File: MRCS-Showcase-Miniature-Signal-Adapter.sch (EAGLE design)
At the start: 4 parts

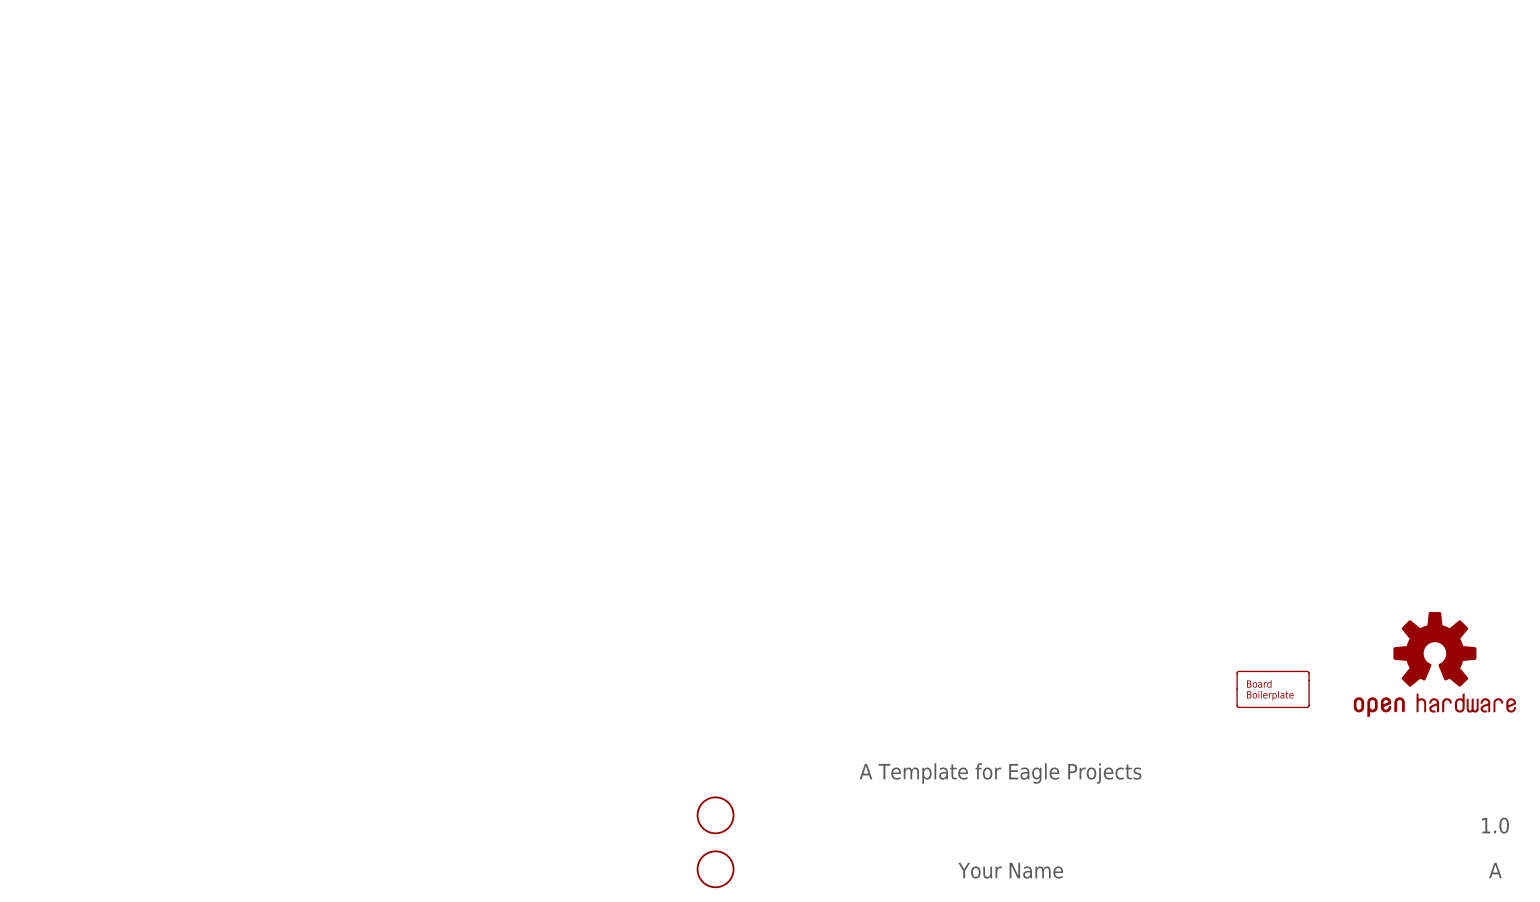
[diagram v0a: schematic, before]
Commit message: Various adjustments of hole and chip sizes
- changed SMD resistors to 1206 to allow easier soldering
- Changed size of shaft hole to match #52 drill
- changes pads to .6mm for better fit with #24 wire
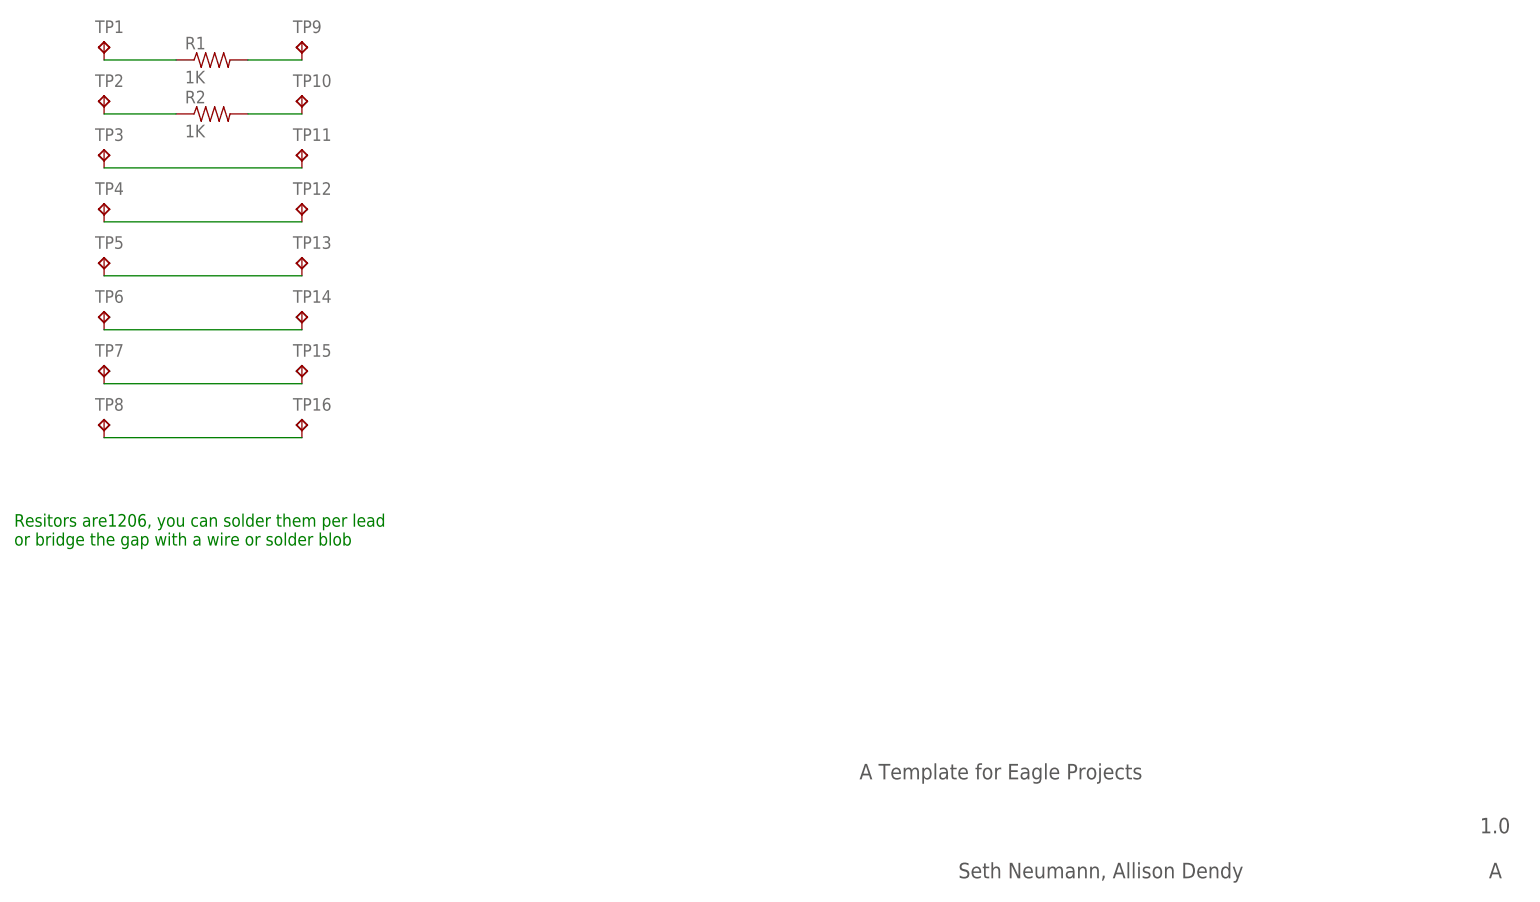
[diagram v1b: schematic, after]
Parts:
- removed BOARD1: BOARD80X100, SPCoast:BOARD80X100
- removed FID1, FID2: FIDUCIAL, SPCoast:FIDUCIAL
- removed OSHW1: DOC-OSHW-LOGO-M, SPCoast:DOC-OSHW-LOGO-M
- added R1, R2: 1K, SPCoast:R1206
- added TP1, TP10, TP11, TP12, TP13, TP14, TP15, TP16, TP2, TP3, TP4, TP5, TP6, TP7, TP8, TP9: TP, MRCS:TP
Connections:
- new net N$10: TP16.TP, TP8.TP
- new net N$17: R1.2, TP9.TP
- new net N$2: R1.1, TP1.TP
- new net N$3: R2.1, TP2.TP
- new net N$4: R2.2, TP10.TP
- new net N$5: TP11.TP, TP3.TP
- new net N$6: TP12.TP, TP4.TP
- new net N$7: TP13.TP, TP5.TP
- new net N$8: TP14.TP, TP6.TP
- new net N$9: TP15.TP, TP7.TP
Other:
- note added: "Resitors are1206, you can solder them per lead or bridge the gap with a wire or solder blob"
- note added: "Seth Neumann, Allison Dendy"
- note removed: "Your Name"
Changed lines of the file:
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@@
 <parts>
 <part name="FRAME1" library="SPCoast" deviceset="DOC-FRAME-LETTER" device=""/>
-<part name="OSHW1" library="SPCoast" deviceset="DOC-OSHW-LOGO-" device="M"/>
-<part name="BOARD1" library="SPCoast" deviceset="BOARD" device="80X100"/>
-<part name="FID2" library="SPCoast" deviceset="FIDUCIAL" device=""/>
-<part name="FID1" library="SPCoast" deviceset="FIDUCIAL" device=""/>
+<part name="R1" library="SPCoast" deviceset="R*" device="1206" value="1K"/>
+<part name="R2" library="SPCoast" deviceset="R*" device="1206" value="1K"/>
+<part name="TP1" library="MRCS" deviceset="TP" device=""/>
+<part name="TP2" library="MRCS" deviceset="TP" device=""/>
+<part name="TP3" library="MRCS" deviceset="TP" device=""/>
+<part name="TP4" library="MRCS" deviceset="TP" device=""/>
+<part name="TP5" library="MRCS" deviceset="TP" device=""/>
+<part name="TP6" library="MRCS" deviceset="TP" device=""/>
+<part name="TP7" library="MRCS" deviceset="TP" device=""/>
+<part name="TP8" library="MRCS" deviceset="TP" device=""/>
+<part name="TP9" library="MRCS" deviceset="TP" device=""/>
+<part name="TP10" library="MRCS" deviceset="TP" device=""/>
+<part name="TP11" library="MRCS" deviceset="TP" device=""/>
+<part name="TP12" library="MRCS" deviceset="TP" device=""/>
+<part name="TP13" library="MRCS" deviceset="TP" device=""/>
+<part name="TP14" library="MRCS" deviceset="TP" device=""/>
+<part name="TP15" library="MRCS" deviceset="TP" device=""/>
+<part name="TP16" library="MRCS" deviceset="TP" device=""/>
 </parts>
 <sheets>
@@
 <text x="240.03" y="12.7" size="2.1844" layer="97">1.0</text>
 <text x="241.3" y="6.35" size="2.1844" layer="97">A</text>
-<text x="166.37" y="6.35" size="2.1844" layer="97">Your Name</text>
+<text x="166.37" y="6.35" size="2.1844" layer="97">Seth Neumann, Allison Dendy</text>
+<text x="33.02" y="53.34" size="1.778" layer="91">Resitors are1206, you can solder them per lead
+or bridge the gap with a wire or solder blob</text>
 </plain>
 <instances>
 <instance part="FRAME1" gate="FRAME" x="0" y="0"/>
 <instance part="FRAME1" gate="FRAME_CONTENT" x="147.32" y="0"/>
-<instance part="OSHW1" gate="DOC-OSHW-LOGO" x="233.68" y="38.1"/>
-<instance part="BOARD1" gate="B" x="210.82" y="33.02"/>
-<instance part="FID2" gate="G$1" x="132.08" y="7.62"/>
-<instance part="FID1" gate="G$1" x="132.08" y="15.24"/>
+<instance part="R1" gate="R" x="60.96" y="121.92"/>
+<instance part="R2" gate="R" x="60.96" y="114.3"/>
+<instance part="TP1" gate="G$1" x="45.72" y="124.46"/>
+<instance part="TP2" gate="G$1" x="45.72" y="116.84"/>
+<instance part="TP3" gate="G$1" x="45.72" y="109.22"/>
+<instance part="TP4" gate="G$1" x="45.72" y="101.6"/>
+<instance part="TP5" gate="G$1" x="45.72" y="93.98"/>
+<instance part="TP6" gate="G$1" x="45.72" y="86.36"/>
+<instance part="TP7" gate="G$1" x="45.72" y="78.74"/>
+<instance part="TP8" gate="G$1" x="45.72" y="71.12"/>
+<instance part="TP9" gate="G$1" x="73.66" y="124.46"/>
+<instance part="TP10" gate="G$1" x="73.66" y="116.84"/>
+<instance part="TP11" gate="G$1" x="73.66" y="109.22"/>
+<instance part="TP12" gate="G$1" x="73.66" y="101.6"/>
+<instance part="TP13" gate="G$1" x="73.66" y="93.98"/>
+<instance part="TP14" gate="G$1" x="73.66" y="86.36"/>
+<instance part="TP15" gate="G$1" x="73.66" y="78.74"/>
+<instance part="TP16" gate="G$1" x="73.66" y="71.12"/>
 </instances>
 <busses>
 </busses>
 <nets>
+<net name="N$2" class="0">
+<segment>
+<pinref part="R1" gate="R" pin="1"/>
+<wire x1="45.72" y1="121.92" x2="55.88" y2="121.92" width="0.3048" layer="91"/>
+<pinref part="TP1" gate="G$1" pin="TP"/>
+</segment>
+</net>
+<net name="N$3" class="0">
+<segment>
+<pinref part="R2" gate="R" pin="1"/>
+<wire x1="45.72" y1="114.3" x2="55.88" y2="114.3" width="0.3048" layer="91"/>
+<pinref part="TP2" gate="G$1" pin="TP"/>
+</segment>
+</net>
+<net name="N$4" class="0">
+<segment>
+<pinref part="R2" gate="R" pin="2"/>
+<wire x1="66.04" y1="114.3" x2="73.66" y2="114.3" width="0.3048" layer="91"/>
+<pinref part="TP10" gate="G$1" pin="TP"/>
+</segment>
+</net>
+<net name="N$17" class="0">
+<segment>
+<pinref part="R1" gate="R" pin="2"/>
+<pinref part="TP9" gate="G$1" pin="TP"/>
+<wire x1="66.04" y1="121.92" x2="73.66" y2="121.92" width="0.3048" layer="91"/>
+</segment>
+</net>
+<net name="N$5" class="0">
+<segment>
+<pinref part="TP3" gate="G$1" pin="TP"/>
+<pinref part="TP11" gate="G$1" pin="TP"/>
+<wire x1="45.72" y1="106.68" x2="73.66" y2="106.68" width="0.3048" layer="91"/>
+</segment>
+</net>
+<net name="N$6" class="0">
+<segment>
+<pinref part="TP4" gate="G$1" pin="TP"/>
+<pinref part="TP12" gate="G$1" pin="TP"/>
+<wire x1="45.72" y1="99.06" x2="73.66" y2="99.06" width="0.3048" layer="91"/>
+</segment>
+</net>
+<net name="N$7" class="0">
+<segment>
+<pinref part="TP5" gate="G$1" pin="TP"/>
+<pinref part="TP13" gate="G$1" pin="TP"/>
+<wire x1="45.72" y1="91.44" x2="73.66" y2="91.44" width="0.3048" layer="91"/>
+</segment>
+</net>
+<net name="N$8" class="0">
+<segment>
+<pinref part="TP6" gate="G$1" pin="TP"/>
+<pinref part="TP14" gate="G$1" pin="TP"/>
+<wire x1="45.72" y1="83.82" x2="73.66" y2="83.82" width="0.3048" layer="91"/>
+</segment>
+</net>
+<net name="N$9" class="0">
+<segment>
+<pinref part="TP7" gate="G$1" pin="TP"/>
+<pinref part="TP15" gate="G$1" pin="TP"/>
+<wire x1="45.72" y1="76.2" x2="73.66" y2="76.2" width="0.3048" layer="91"/>
+</segment>
+</net>
+<net name="N$10" class="0">
+<segment>
+<pinref part="TP8" gate="G$1" pin="TP"/>
+<pinref part="TP16" gate="G$1" pin="TP"/>
+<wire x1="45.72" y1="68.58" x2="73.66" y2="68.58" width="0.3048" layer="91"/>
+</segment>
+</net>
 </nets>
 </sheet>
